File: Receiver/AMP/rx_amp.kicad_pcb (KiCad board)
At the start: 2 copper layers, 30 x 30 mm, 12 parts, among them IC1 BGA616H6327XTSA1, J1 Conn_Coaxial, J2 Conn_Coaxial, J3 Screw_Terminal_01x02

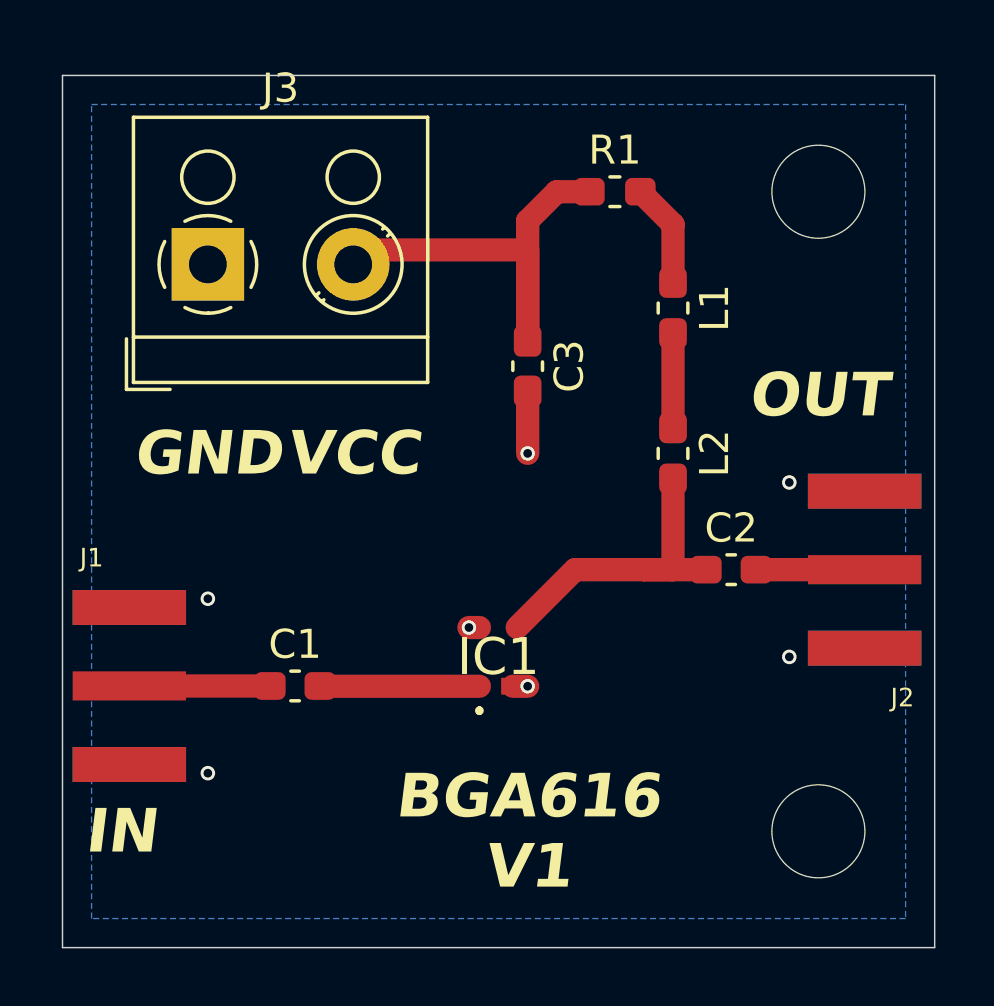
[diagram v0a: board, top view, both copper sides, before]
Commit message: Updated Rx Symbol Fields.
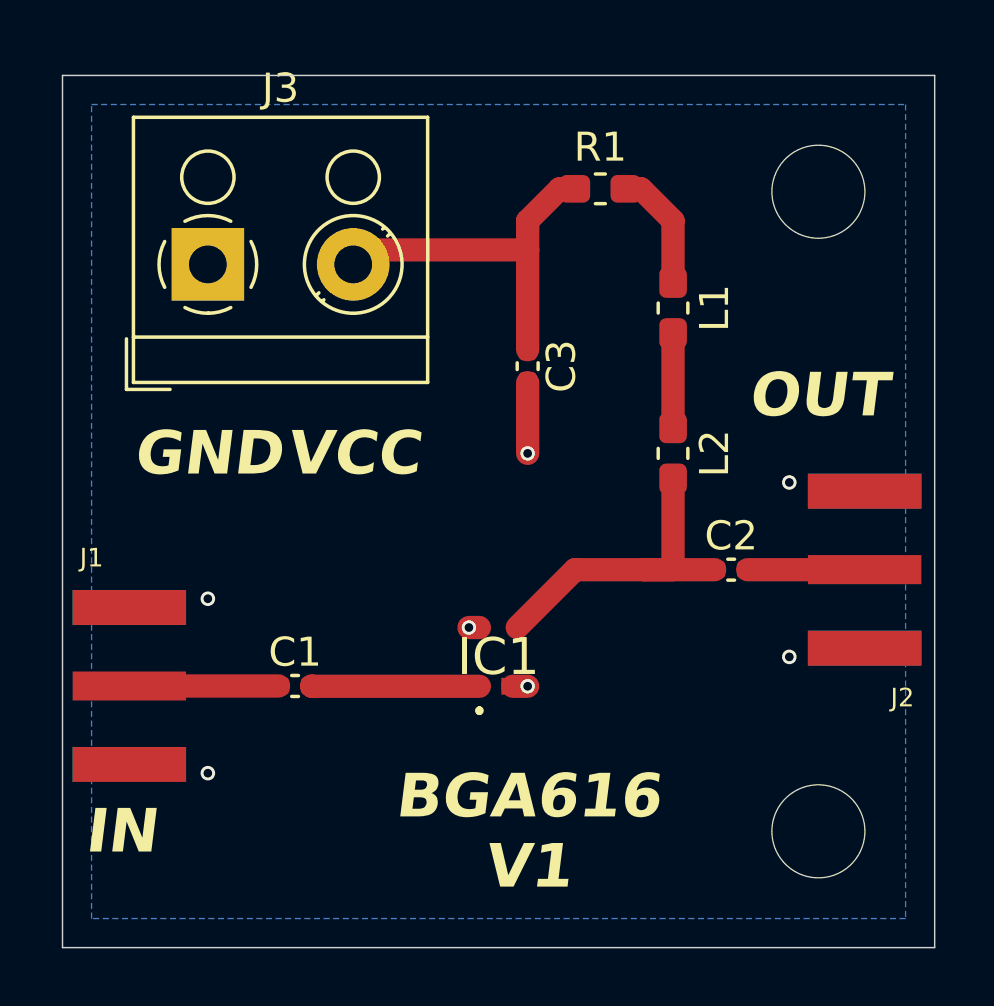
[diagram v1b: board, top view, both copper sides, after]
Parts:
- C1, C2, C3: footprint Capacitor_SMD:C_0603_1608Metric_Pad1.08x0.95mm_HandSolder -> Capacitor_SMD:C_0402_1005Metric_Pad0.74x0.62mm_HandSolder
- H1, H3: value m3 -> M3 mounting hole
- J1: value Conn_Coaxial -> Signal_In
- J2: value Conn_Coaxial -> Signal_Out
- moved R1 0.51 mm to (128.5, 93.9)
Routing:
- net Net-(J3-Pin_2): track 16.0 -> 12.7 mm
- net Net-(L1-Pad1): track 3.59 -> 4.21 mm

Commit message: Updated FCA symbols
Updated FCA symbols with mouser number parts.
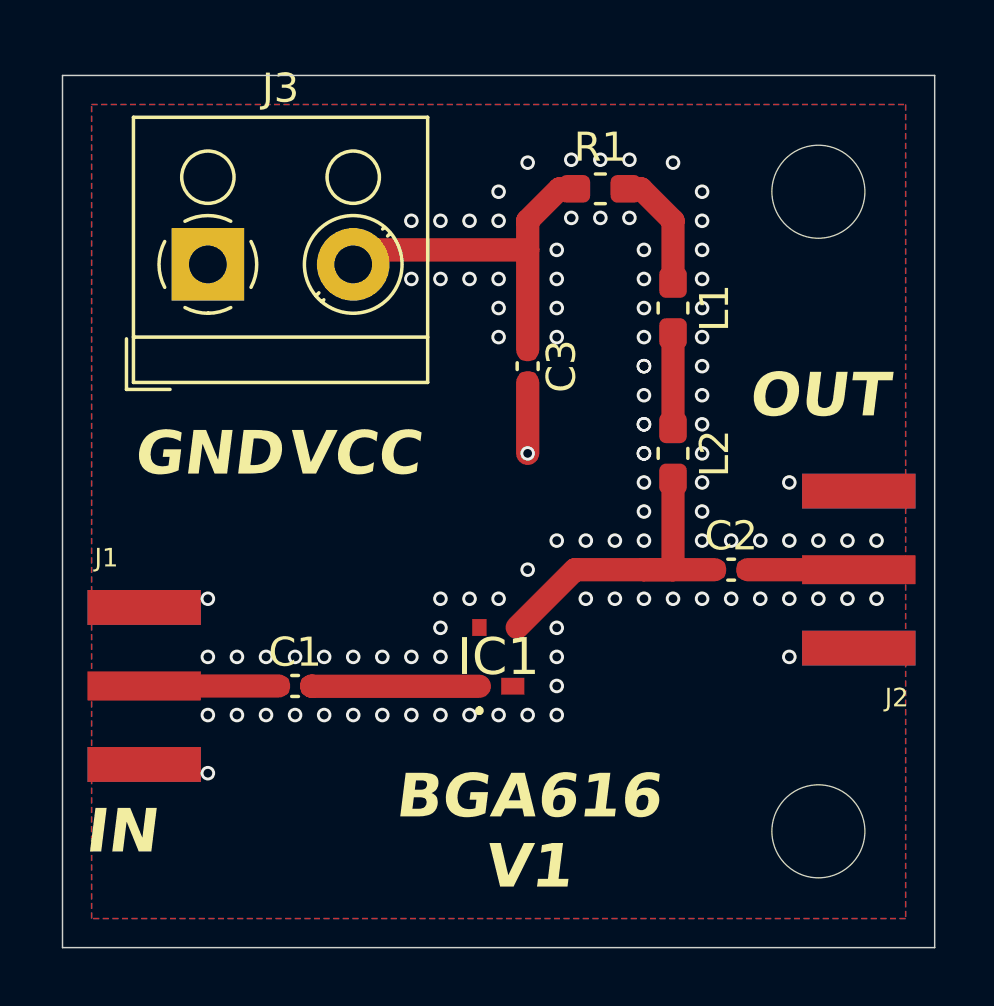
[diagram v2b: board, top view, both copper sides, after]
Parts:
- moved J1 0.51 mm to (111.5, 111.0)
- moved J2 0.20 mm to (138.7, 107.0)
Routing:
- net GND: track 3.30 -> 2.43 mm, vias 7 -> 105
- added copper zone on F.Cu, net GND

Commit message: Rx Amp first version
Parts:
- added L3: Ferrite Beads 220 OHM, Inductor_SMD:L_0603_1608Metric_Pad1.05x0.95mm_HandSolder, F.Cu at (125.0, 96.0)
- C1, C2, C3: value 10nF -> .1uF
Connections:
- C3 pad 1: Net-(J3-Pin_2) -> Net-(C3-Pad1)
- R1 pad 1: Net-(J3-Pin_2) -> Net-(C3-Pad1)
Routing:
- net Net-(J3-Pin_2): track 12.7 -> 4.33 mm
- net Net-(C3-Pad1): track 0.00 -> 6.51 mm
- net GND: vias 105 -> 96

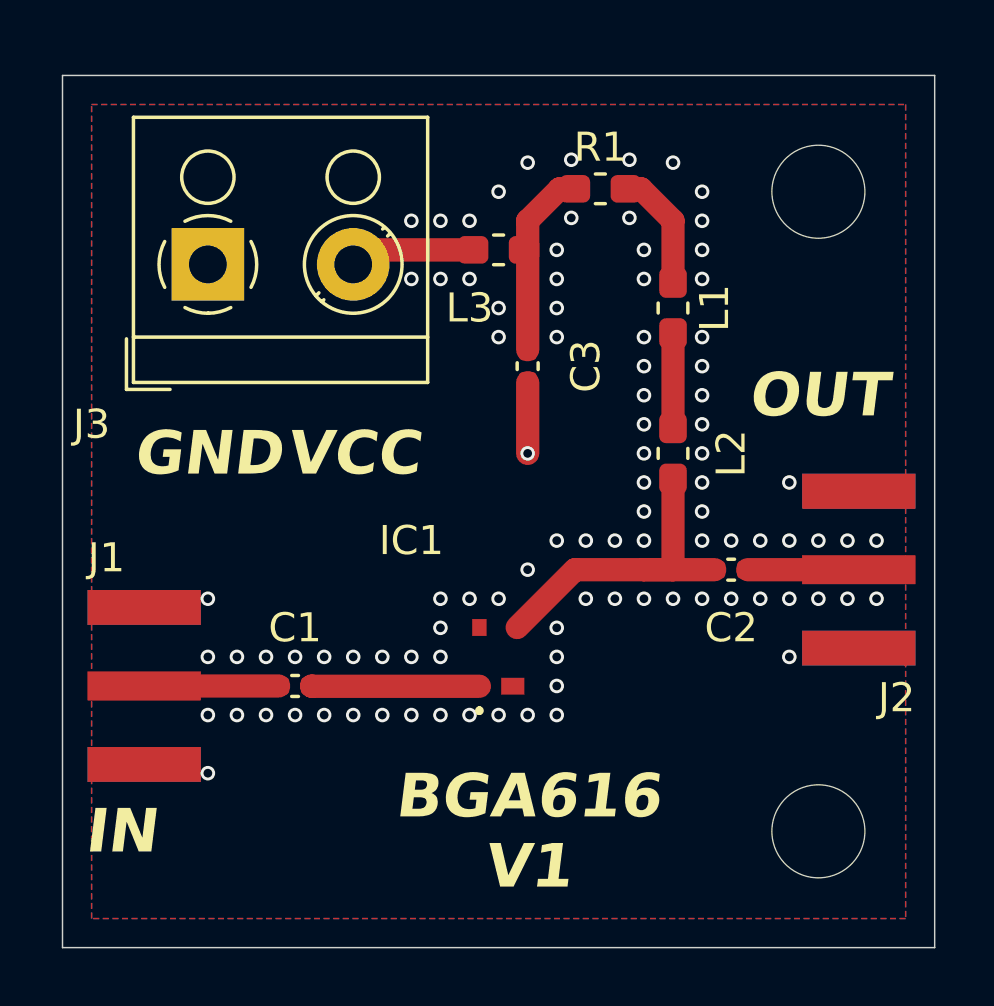
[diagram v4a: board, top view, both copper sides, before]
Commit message: SMA footprint rx-amp fixed
SMA footprint rx-amp fixed
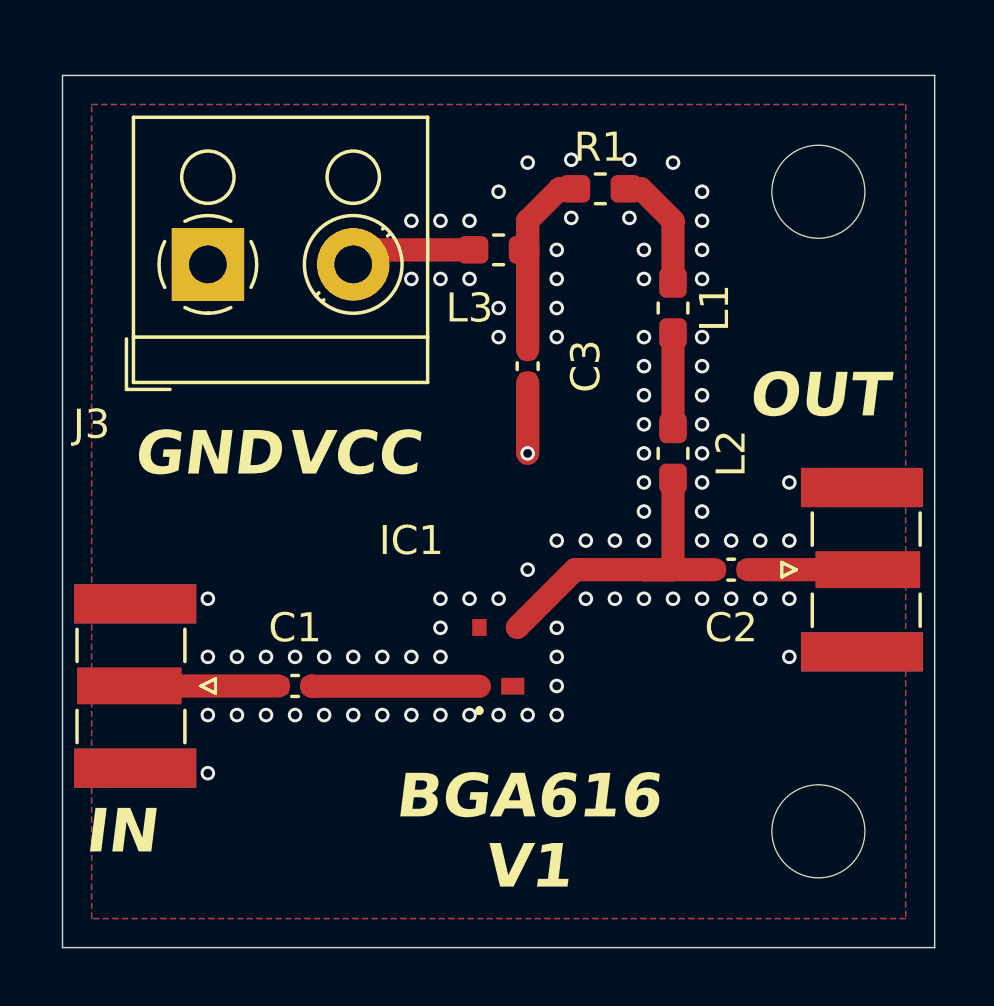
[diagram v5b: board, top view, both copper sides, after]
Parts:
- J1, J2: footprint rx_amp:RFSOLUTIONS_CON-SMA-EDGE-S -> Connector_Coaxial:SMA_Samtec_SMA-J-P-X-ST-EM1_EdgeMount
- moved J2 1.19 mm to (137.5, 107.0), turned to 90 degrees
- moved J1 0.99 mm to (112.5, 111.0), turned to -90 degrees
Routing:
- net GND: vias 96 -> 90

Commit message: Receiver AMP updated ibom and gerber
Receiver AMP updated ibom and gerber
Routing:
- net GND: track 2.43 -> 0.00 mm, vias 90 -> 89
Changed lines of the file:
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@@
 		(tags "SMA Straight Samtec Edge Mount")
 		(property "Reference" "J2"
-			(at 0 -3.5 270)
+			(at 0 -3.5 -90)
 			(layer "F.SilkS")
 			(hide yes)
@@
 		)
 		(property "Value" "Signal_Out"
-			(at 0 13 270)
+			(at 0 13 -90)
 			(layer "F.Fab")
 			(effects
@@
 		)
 		(fp_line
-			(start -4 -2.600001)
-			(end 4 -2.600001)
+			(start -4 -2.6)
+			(end 4 -2.6)
 			(stroke
 				(width 0.05)
@@
 		)
 		(fp_line
-			(start 4 2.600001)
-			(end 4 -2.600001)
+			(start 4 2.6)
+			(end 4 -2.6)
 			(stroke
 				(width 0.05)
@@
 		)
 		(fp_line
-			(start 4 2.600001)
-			(end 3.68 2.600001)
+			(start 4 2.6)
+			(end 3.68 2.6)
 			(stroke
 				(width 0.05)
@@
 		)
 		(fp_line
-			(start 3.68 2.600001)
+			(start 3.68 2.6)
 			(end 3.68 12.12)
 			(stroke
@@
 		)
 		(fp_line
-			(start -3.68 2.600001)
-			(end -4 2.600001)
+			(start -3.68 2.6)
+			(end -4 2.6)
 			(stroke
 				(width 0.05)
@@
 		)
 		(fp_line
-			(start -4 2.600001)
-			(end -4 -2.600001)
+			(start -4 2.6)
+			(end -4 -2.6)
 			(stroke
 				(width 0.05)
@@
 		(fp_line
 			(start -3.68 12.12)
-			(end -3.68 2.600001)
+			(end -3.68 2.6)
 			(stroke
 				(width 0.05)
@@
 		)
 		(fp_line
-			(start -4 -2.600001)
-			(end 4 -2.600001)
+			(start -4 -2.6)
+			(end 4 -2.6)
 			(stroke
 				(width 0.05)
@@
 		)
 		(fp_line
-			(start 4 2.600001)
-			(end 4 -2.600001)
+			(start 4 2.6)
+			(end 4 -2.6)
 			(stroke
 				(width 0.05)
@@
 		)
 		(fp_line
-			(start 3.68 2.600001)
-			(end 4 2.600001)
+			(start 3.68 2.6)
+			(end 4 2.6)
 			(stroke
 				(width 0.05)
@@
 		)
 		(fp_line
-			(start 3.68 2.600001)
+			(start 3.68 2.6)
 			(end 3.68 12.12)
 			(stroke
@@
 		)
 		(fp_line
-			(start -3.68 2.600001)
-			(end -4 2.600001)
+			(start -3.68 2.6)
+			(end -4 2.6)
 			(stroke
 				(width 0.05)
@@
 		)
 		(fp_line
-			(start -4 2.600001)
-			(end -4 -2.600001)
+			(start -4 2.6)
+			(end -4 -2.6)
 			(stroke
 				(width 0.05)
@@
 		(fp_line
 			(start -3.68 12.12)
-			(end -3.68 2.600001)
+			(end -3.68 2.6)
 			(stroke
 				(width 0.05)
@@
 		)
 		(fp_line
-			(start 3.175 -1.710001)
+			(start 3.175 -1.71)
 			(end 2.365 -1.71)
 			(stroke
@@
 		)
 		(fp_line
-			(start 3.175 -1.710001)
+			(start 3.175 -1.71)
 			(end 3.175 11.62)
 			(stroke
@@
 		)
 		(fp_line
-			(start -3.175 -1.710001)
-			(end -3.175 11.62)
+			(start 2.365 -1.71)
+			(end 2.365 2.1)
 			(stroke
 				(width 0.1)
@@
 		)
 		(fp_line
-			(start 2.365 -1.71)
-			(end 2.365 2.1)
+			(start -2.365 -1.71)
+			(end -3.175 -1.71)
 			(stroke
 				(width 0.1)
@@
 		)
 		(fp_line
-			(start -2.365 -1.71)
-			(end -3.175 -1.710001)
+			(start -3.175 -1.71)
+			(end -3.175 11.62)
 			(stroke
 				(width 0.1)
@@
 		)
 		(fp_text user "PCB Edge"
-			(at 0 2.600001 270)
+			(at 0 2.600001 -90)
 			(layer "Dwgs.User")
 			(effects
@@
 		)
 		(fp_text user "Board Thickness: 1.57mm"
-			(at 0 -5.45 270)
+			(at 0 -5.45 -90)
 			(layer "Cmts.User")
 			(effects
@@
 		)
 		(fp_text user "${REFERENCE}"
-			(at 0 4.789999 270)
+			(at 0 4.789999 -90)
 			(layer "F.Fab")
 			(effects
@@
 		)
 		(pad "1" smd rect
-			(at 0 0.199999 90)
+			(at 0 0.2 90)
 			(size 1.27 3.6)
 			(layers "F.Cu" "F.Paste" "F.Mask")
@@
 		(fp_line
 			(start -3.68 12.12)
-			(end -3.68 2.600001)
+			(end -3.68 2.6)
 			(stroke
 				(width 0.05)
@@
 		)
 		(fp_line
-			(start -4 2.600001)
-			(end -4 -2.600001)
+			(start -4 2.6)
+			(end -4 -2.6)
 			(stroke
 				(width 0.05)
@@
 		)
 		(fp_line
-			(start -3.68 2.600001)
-			(end -4 2.600001)
+			(start -3.68 2.6)
+			(end -4 2.6)
 			(stroke
 				(width 0.05)
@@
 		)
 		(fp_line
-			(start 3.68 2.600001)
+			(start 3.68 2.6)
 			(end 3.68 12.12)
 			(stroke
@@
 		)
 		(fp_line
-			(start 4 2.600001)
-			(end 3.68 2.600001)
+			(start 4 2.6)
+			(end 3.68 2.6)
 			(stroke
 				(width 0.05)
@@
 		)
 		(fp_line
-			(start 4 2.600001)
-			(end 4 -2.600001)
+			(start 4 2.6)
+			(end 4 -2.6)
 			(stroke
 				(width 0.05)
@@
 		)
 		(fp_line
-			(start -4 -2.600001)
-			(end 4 -2.600001)
+			(start -4 -2.6)
+			(end 4 -2.6)
 			(stroke
 				(width 0.05)
@@
 		(fp_line
 			(start -3.68 12.12)
-			(end -3.68 2.600001)
+			(end -3.68 2.6)
 			(stroke
 				(width 0.05)
@@
 		)
 		(fp_line
-			(start -4 2.600001)
-			(end -4 -2.600001)
+			(start -4 2.6)
+			(end -4 -2.6)
 			(stroke
 				(width 0.05)
@@
 		)
 		(fp_line
-			(start -3.68 2.600001)
-			(end -4 2.600001)
+			(start -3.68 2.6)
+			(end -4 2.6)
 			(stroke
 				(width 0.05)
@@
 		)
 		(fp_line
-			(start 3.68 2.600001)
+			(start 3.68 2.6)
 			(end 3.68 12.12)
 			(stroke
@@
 		)
 		(fp_line
-			(start 3.68 2.600001)
-			(end 4 2.600001)
+			(start 3.68 2.6)
+			(end 4 2.6)
 			(stroke
 				(width 0.05)
@@
 		)
 		(fp_line
-			(start 4 2.600001)
-			(end 4 -2.600001)
+			(start 4 2.6)
+			(end 4 -2.6)
 			(stroke
 				(width 0.05)
@@
 		)
 		(fp_line
-			(start -4 -2.600001)
-			(end 4 -2.600001)
+			(start -4 -2.6)
+			(end 4 -2.6)
 			(stroke
 				(width 0.05)
@@
 		)
 		(fp_line
-			(start -2.365 -1.71)
-			(end -3.175 -1.710001)
+			(start -3.175 -1.71)
+			(end -3.175 11.62)
 			(stroke
 				(width 0.1)
@@
 		)
 		(fp_line
-			(start 2.365 -1.71)
-			(end 2.365 2.1)
+			(start -2.365 -1.71)
+			(end -3.175 -1.71)
 			(stroke
 				(width 0.1)
@@
 		)
 		(fp_line
-			(start -3.175 -1.710001)
-			(end -3.175 11.62)
+			(start 2.365 -1.71)
+			(end 2.365 2.1)
 			(stroke
 				(width 0.1)
@@
 		)
 		(fp_line
-			(start 3.175 -1.710001)
+			(start 3.175 -1.71)
 			(end 3.175 11.62)
 			(stroke
@@
 		)
 		(fp_line
-			(start 3.175 -1.710001)
+			(start 3.175 -1.71)
 			(end 2.365 -1.71)
 			(stroke
@@
 		)
 		(pad "1" smd rect
-			(at 0 0.199999 270)
+			(at 0 0.2 270)
 			(size 1.27 3.6)
 			(layers "F.Cu" "F.Paste" "F.Mask")
@@
 		(attr smd)
 		(fp_line
-			(start -0.171268 0.51)
-			(end 0.171268 0.51)
+			(start -0.171267 0.51)
+			(end 0.171267 0.51)
 			(stroke
 				(width 0.12)
@@
 		)
 		(fp_line
-			(start -0.171268 -0.51)
-			(end 0.171268 -0.51)
+			(start -0.171267 -0.51)
+			(end 0.171267 -0.51)
 			(stroke
 				(width 0.12)
@@
 		)
 		(pad "1" smd roundrect
-			(at -0.874999 0 270)
+			(at -0.875 0 270)
 			(size 1.05 0.95)
 			(layers "F.Cu" "F.Paste" "F.Mask")
@@
 		)
 		(pad "2" smd roundrect
-			(at 0.874999 0 270)
+			(at 0.875 0 270)
 			(size 1.05 0.95)
 			(layers "F.Cu" "F.Paste" "F.Mask")
@@
 		(attr smd)
 		(fp_line
-			(start -0.171268 0.51)
-			(end 0.171268 0.51)
+			(start -0.171267 0.51)
+			(end 0.171267 0.51)
 			(stroke
 				(width 0.12)
@@
 		)
 		(fp_line
-			(start -0.171268 -0.51)
-			(end 0.171268 -0.51)
+			(start -0.171267 -0.51)
+			(end 0.171267 -0.51)
 			(stroke
 				(width 0.12)
@@
 		)
 		(pad "1" smd roundrect
-			(at -0.874999 0 270)
+			(at -0.875 0 270)
 			(size 1.05 0.95)
 			(layers "F.Cu" "F.Paste" "F.Mask")
@@
 		)
 		(pad "2" smd roundrect
-			(at 0.874999 0 270)
+			(at 0.875 0 270)
 			(size 1.05 0.95)
 			(layers "F.Cu" "F.Paste" "F.Mask")
@@
 		(net 4)
 	)
-	(segment
-		(start 126 103)
-		(end 126 100.5675)
-		(width 0.8)
-		(layer "F.Cu")
-		(net 5)
-	)
 	(via
 		(at 122 110)
@@
 		(net 5)
 	)
-	(via
-		(at 126 103)
-		(size 0.5)
-		(drill 0.3)
-		(layers "F.Cu" "B.Cu")
-		(net 5)
-	)
